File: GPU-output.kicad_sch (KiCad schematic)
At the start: 23 parts, among them J1 Conn_1-2212115-4, Q1 BSS138PW, Q2 SI7613DN-T1-GE3, Q3 SI7613DN-T1-GE3, U4 TMCS1100A2-Q1

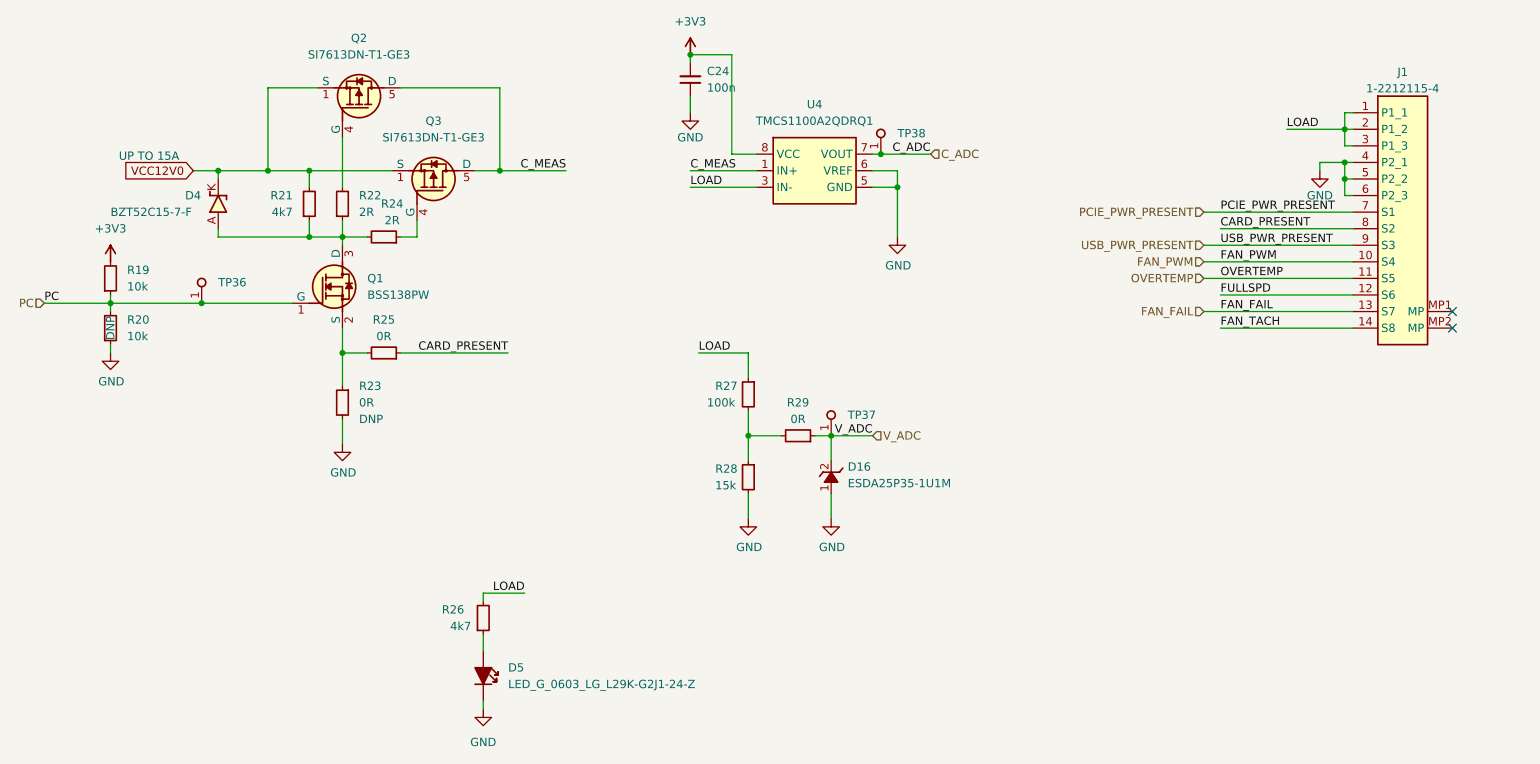
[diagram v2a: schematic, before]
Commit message: Placement of supply section on PCB
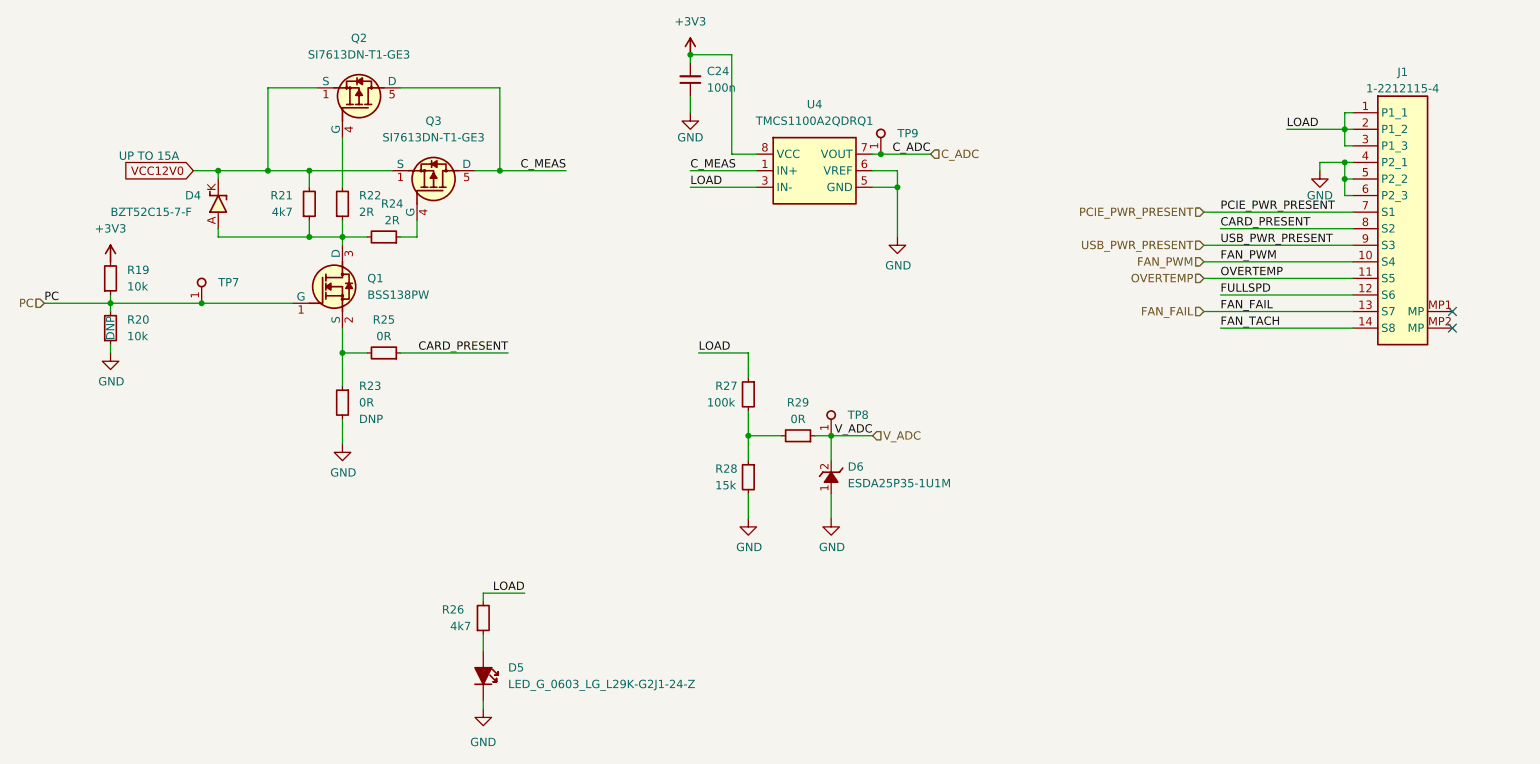
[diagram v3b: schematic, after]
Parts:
- renumbered D16 to D6, TP36 to TP7, TP37 to TP8, TP38 to TP9
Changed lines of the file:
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@@
   (symbol (lib_id "antmicroTestPoints:TP_1mm_SMD") (at 233.68 110.49 90) (unit 1)
     (in_bom yes) (on_board yes) (fields_autoplaced)
-    (property "Reference" "TP38" (id 0) (at 236.22 107.3149 90)
+    (property "Reference" "TP9" (id 0) (at 236.22 107.3149 90)
       (effects (font (size 1.27 1.27) (thickness 0.15)) (justify right))
     )
@@
   (symbol (lib_id "antmicroTVSDiodes:ESDA25P35-1U1M") (at 226.06 162.56 90) (unit 1)
     (in_bom yes) (on_board yes) (fields_autoplaced)
-    (property "Reference" "D16" (id 0) (at 228.6 158.4324 90)
+    (property "Reference" "D6" (id 0) (at 228.6 158.4324 90)
       (effects (font (size 1.27 1.27) (thickness 0.15)) (justify right))
     )
@@
   (symbol (lib_id "antmicropower:GND") (at 236.22 123.19 0) (unit 1)
     (in_bom yes) (on_board yes)
-    (property "Reference" "#PWR048" (id 0) (at 236.22 129.54 0)
+    (property "Reference" "#PWR049" (id 0) (at 236.22 129.54 0)
       (effects (font (size 1.27 1.27)) hide)
     )
@@
   (symbol (lib_id "antmicroTestPoints:TP_1mm_SMD") (at 226.06 153.67 90) (unit 1)
     (in_bom yes) (on_board yes) (fields_autoplaced)
-    (property "Reference" "TP37" (id 0) (at 228.6 150.4949 90)
+    (property "Reference" "TP8" (id 0) (at 228.6 150.4949 90)
       (effects (font (size 1.27 1.27) (thickness 0.15)) (justify right))
     )
@@
   (symbol (lib_id "antmicropower:GND") (at 226.06 166.37 0) (unit 1)
     (in_bom yes) (on_board yes)
-    (property "Reference" "#PWR0139" (id 0) (at 226.06 172.72 0)
+    (property "Reference" "#PWR048" (id 0) (at 226.06 172.72 0)
       (effects (font (size 1.27 1.27)) hide)
     )
@@
   (symbol (lib_id "antmicroTestPoints:TP_1mm_SMD") (at 129.54 133.35 90) (unit 1)
     (in_bom yes) (on_board yes) (fields_autoplaced)
-    (property "Reference" "TP36" (id 0) (at 132.08 130.1749 90)
+    (property "Reference" "TP7" (id 0) (at 132.08 130.1749 90)
       (effects (font (size 1.27 1.27) (thickness 0.15)) (justify right))
     )
@@
   (symbol (lib_id "antmicropower:GND") (at 300.99 113.03 0) (unit 1)
     (in_bom yes) (on_board yes)
-    (property "Reference" "#PWR049" (id 0) (at 300.99 119.38 0)
-      (effects (font (size 1.27 1.27)) hide)
-    )
+    (property "Reference" "#PWR050" (id 0) (at 300.99 119.38 0)
+      (effects (font (size 1.27 1.27)) hide)
+    )

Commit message: Start routing of GPIO/ADC circuit
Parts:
- added C96: C_100n_0402, antmicro-footprints:C_0402_1005Metric, symbol antmicroCapacitors0402:C_100n_0402
- added R291: R_10k_0402, antmicro-footprints:R_0402_1005Metric, symbol antmicroResistors0402:R_10k_0402
- added U33: SN74LV1T125DBVR, antmicro-footprints:SOT-23-5, symbol antmicroLogicBuffersDriversReceiversTransceivers:SN74LV1T125DBVR
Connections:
- net CARD_PRESENT: now also J1.12 (S6); no longer J1.8 (S2)
- net FAN_FAIL: now also J1.9 (S3); no longer J1.13 (S7)
- net FAN_PWM: now also U33.4 (Y); no longer J1.10 (S4)
- net FAN_TACH: now also J1.10 (S4); no longer J1.14 (S8)
- net FULLSPD: now also J1.8 (S2); no longer J1.12 (S6)
- net GND: now also J1.1 (P1_1), J1.2 (P1_2), J1.3 (P1_3), C96.1, U33.1 (~{OE}), U33.3 (GND); no longer J1.4 (P2_1), J1.5 (P2_2), J1.6 (P2_3)
- net LOAD: now also J1.4 (P2_1), J1.5 (P2_2), J1.6 (P2_3); no longer J1.1 (P1_1), J1.2 (P1_2), J1.3 (P1_3)
- net OVERTEMP: now also J1.7 (S1); no longer J1.11 (S5)
- net PCIE_PWR_PRESENT: now also J1.11 (S5); no longer J1.7 (S1)
- net USB_PWR_PRESENT: now also J1.13 (S7); no longer J1.9 (S3)
- new net +5V: C96.2, R291.2, U33.5 (VCC)
- new net FAN_PWM_INTERNAL: J1.14 (S8), R291.1, U33.2 (A)

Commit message: Implement changes suggested in schematic review
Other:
- company: (none) -> Antmicro Ltd
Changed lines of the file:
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@@
   (title_block
     (title "GPU Cluster Backplane")
-    (date "2023-10-18")
+    (date "2023-11-09")
     (rev "1.0.0")
+    (company "Antmicro Ltd")
     (comment 1 "www.antmicro.com")
-    (comment 2 "Antmicro Ltd.")
   )
   (junction (at 175.26 113.03) (diameter 0) (color 0 0 0 0)

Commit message: 2nd part of review changes
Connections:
- net FAN_TACH: no longer names the net of J1.10 (S4)
- net FULLSPD: no longer names the net of J1.8 (S2)
- net LOAD renamed P2
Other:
- note added: "FAN_TACH"
- note added: "FULLSPD"
- moved on the sheet: C24

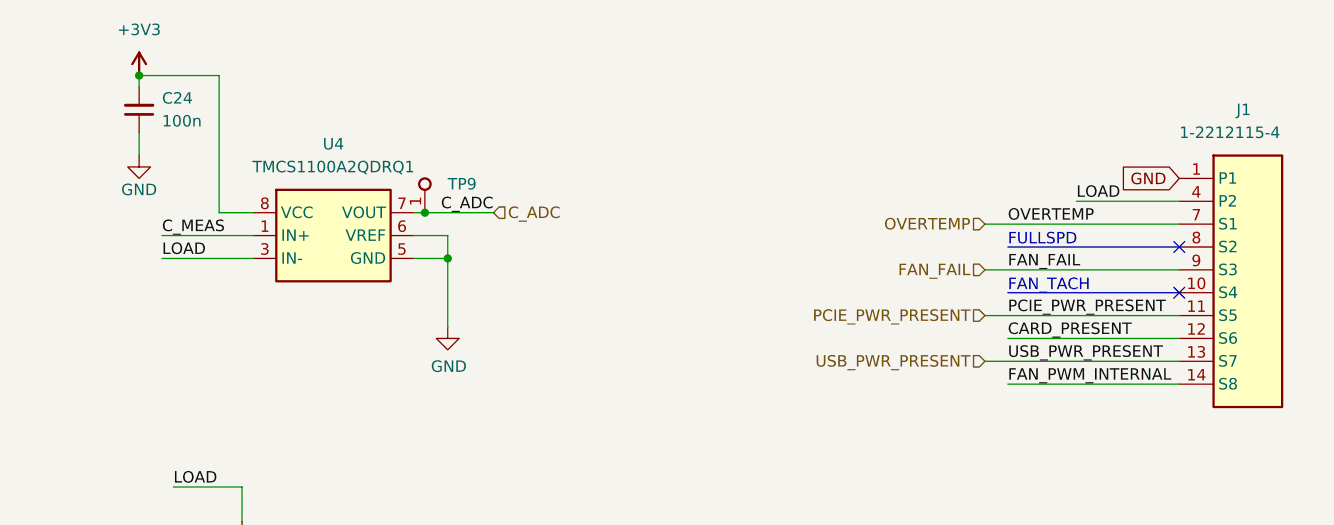
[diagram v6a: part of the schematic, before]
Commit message: Cleaning ERC on schematic
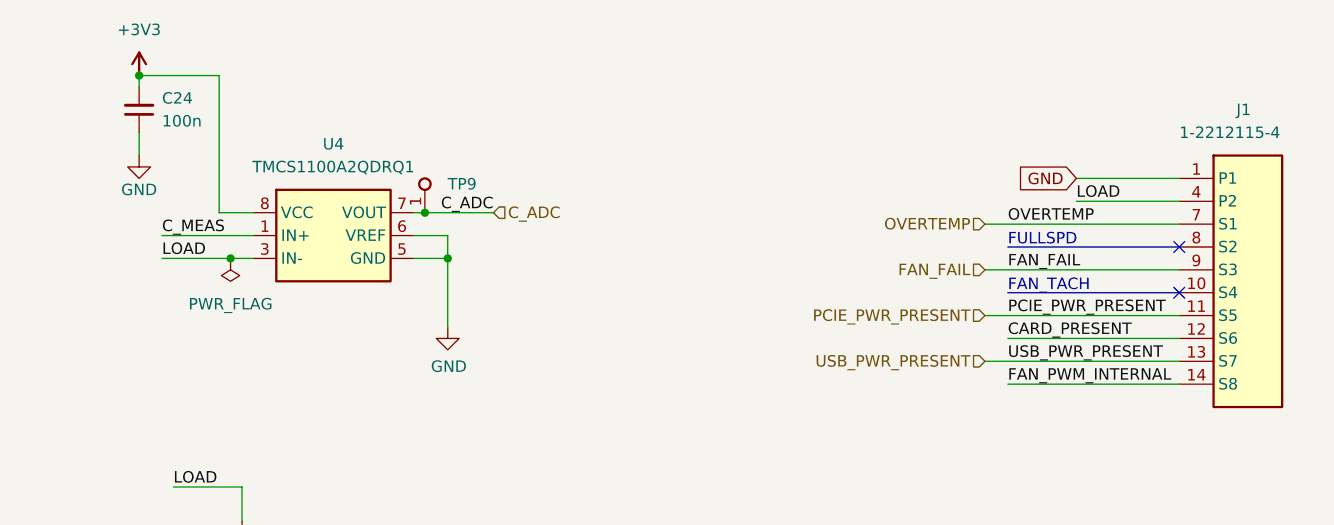
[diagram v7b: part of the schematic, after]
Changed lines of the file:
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@@
     (comment 1 "www.antmicro.com")
   )
+  (junction (at 212.09 115.57) (diameter 0) (color 0 0 0 0)
+  )
   (junction (at 175.26 113.03) (diameter 0) (color 0 0 0 0)
   )
@@
     (stroke (width 0) (type default) (color 0 0 0 0))
   )
+  (wire (pts (xy 204.47 115.57) (xy 212.09 115.57))
+    (stroke (width 0) (type default) (color 0 0 0 0))
+  )
   (wire (pts (xy 201.93 95.25) (xy 201.93 96.52))
     (stroke (width 0) (type default) (color 0 0 0 0))
@@
     (stroke (width 0) (type default) (color 0 0 0 0))
   )
+  (wire (pts (xy 212.09 115.57) (xy 214.63 115.57))
+    (stroke (width 0) (type default) (color 0 0 0 0))
+  )
   (wire (pts (xy 226.06 153.67) (xy 232.41 153.67))
     (stroke (width 0) (type default) (color 0 0 0 0))
@@
     (stroke (width 0) (type default) (color 0 0 0 0))
   )
-  (wire (pts (xy 204.47 115.57) (xy 214.63 115.57))
-    (stroke (width 0) (type default) (color 0 0 0 0))
-  )
   (wire (pts (xy 266.7 151.13) (xy 266.7 152.4))
     (stroke (width 0) (type default) (color 0 0 0 0))
@@
     (stroke (width 0) (type default) (color 0 0 0 0))
   )
+  (wire (pts (xy 306.07 106.68) (xy 317.5 106.68))
+    (stroke (width 0) (type default) (color 0 0 0 0))
+  )
   (wire (pts (xy 139.7 100.33) (xy 147.32 100.33))
     (stroke (width 0) (type default) (color 0 0 0 0))
@@
     (effects (font (size 1.27 1.27)) (justify left bottom))
   )
-  (global_label "GND" (shape input) (at 317.5 106.68 180) (fields_autoplaced)
+  (global_label "GND" (shape input) (at 306.07 106.68 180) (fields_autoplaced)
     (effects (font (size 1.27 1.27)) (justify right))
-    (property "Intersheet References" "${INTERSHEET_REFS}" (id 0) (at 311.3053 106.6006 0)
+    (property "Intersheet References" "${INTERSHEET_REFS}" (id 0) (at 299.8753 106.6006 0)
       (effects (font (size 1.27 1.27)) (justify right) hide)
     )
@@
     (pin "2")
   )
+  (symbol (lib_id "antmicropower:PWR_FLAG") (at 212.09 115.57 180) (unit 1)
+    (in_bom yes) (on_board yes) (fields_autoplaced)
+    (property "Reference" "#FLG0101" (id 0) (at 212.09 117.475 0)
+      (effects (font (size 1.27 1.27)) hide)
+    )
+    (property "Value" "PWR_FLAG" (id 1) (at 212.09 120.65 0))
+    (property "Footprint" "" (id 2) (at 212.09 115.57 0)
+      (effects (font (size 1.27 1.27)) hide)
+    )
+    (property "Datasheet" "" (id 3) (at 212.09 115.57 0)
+      (effects (font (size 1.27 1.27)) hide)
+    )
+    (pin "1")
+  )
   (symbol (lib_id "antmicropower:GND") (at 236.22 123.19 0) (unit 1)
